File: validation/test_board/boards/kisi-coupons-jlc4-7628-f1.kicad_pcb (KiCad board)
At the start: 4 copper layers, 50 x 96 mm, 16 parts, among them J1 292-J-P-EP-ST-EL-01, J10 292-J-P-EP-ST-EL-01, J11 292-J-P-EP-ST-EL-01, J12 292-J-P-EP-ST-EL-01, J13 292-J-P-EP-ST-EL-01, J14 292-J-P-EP-ST-EL-01, J15 292-J-P-EP-ST-EL-01, J16 292-J-P-EP-ST-EL-01, J2 292-J-P-EP-ST-EL-01, J3 292-J-P-EP-ST-EL-01, J4 292-J-P-EP-ST-EL-01, J5 292-J-P-EP-ST-EL-01, J6 292-J-P-EP-ST-EL-01, J7 292-J-P-EP-ST-EL-01, J8 292-J-P-EP-ST-EL-01, J9 292-J-P-EP-ST-EL-01

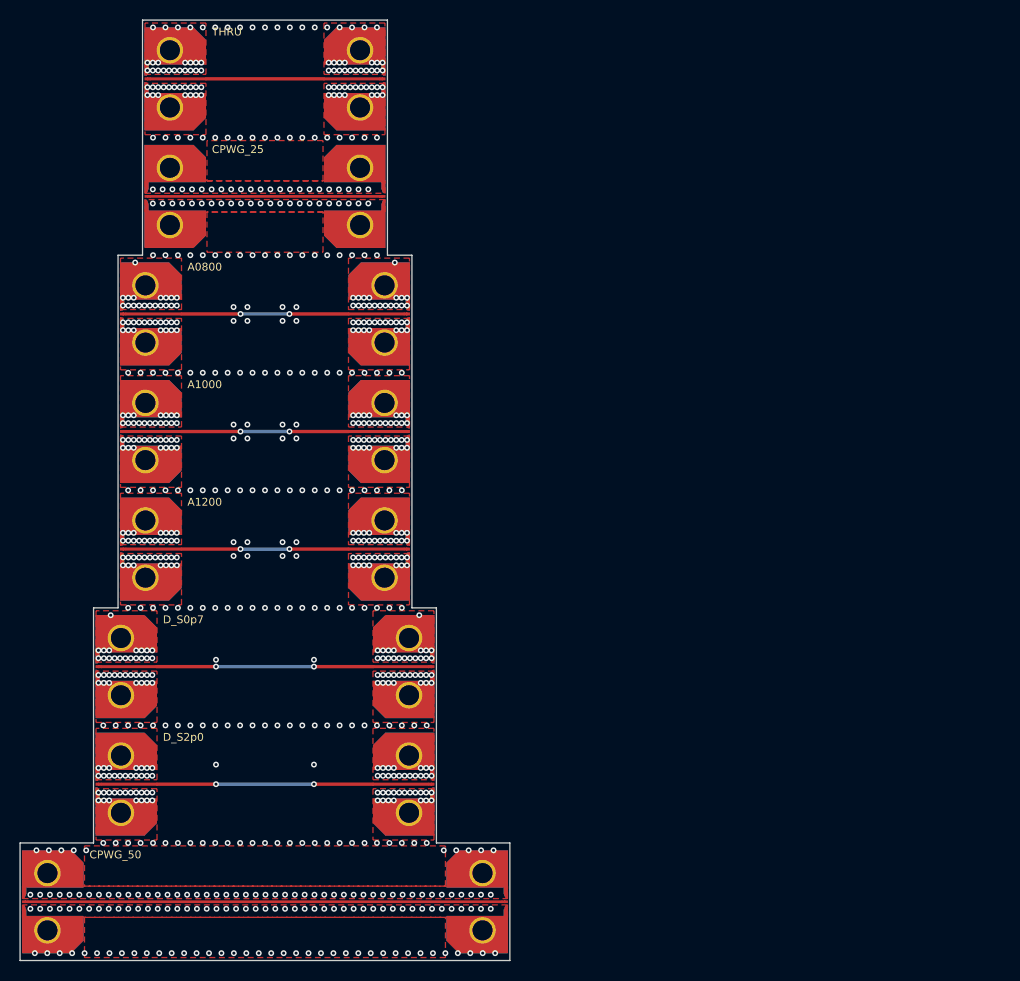
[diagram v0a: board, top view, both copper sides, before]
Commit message: First order: two 4-layer boards and one 6-layer board
- Maintainer's layout (2026-10-31): jlc4-7628-f1 100 x 96 mm (THRU,
  CPWG L / 2L, XT_MS, G_CAV), jlc4-7628-f2 35 x 156 mm (THRU, A x 3,
  D 0.7 / 2 mm / none, PAIR, E with 2 and 0 GND vias), jlc6-7628-f1
  50 x 132 mm (THRU, SL_L3 / VLV_L3, B_L1L6, PAIR, E_R_G2, D x 3). One
  2x-thru per board. An edge launch needs 12 mm of edge per connector
  and side, so the 4-layer set cannot share one 100 x 100 mm board; the
  two boards above their price bracket get their own size limits.
- DRC (KiCad 7, converted copies): no errors; kisi check rerun; the
  first-order table in test_board.md and README lists the exact sizes.

Co-Authored-By: Claude Opus 5.5 <noreply@anthropic.com>
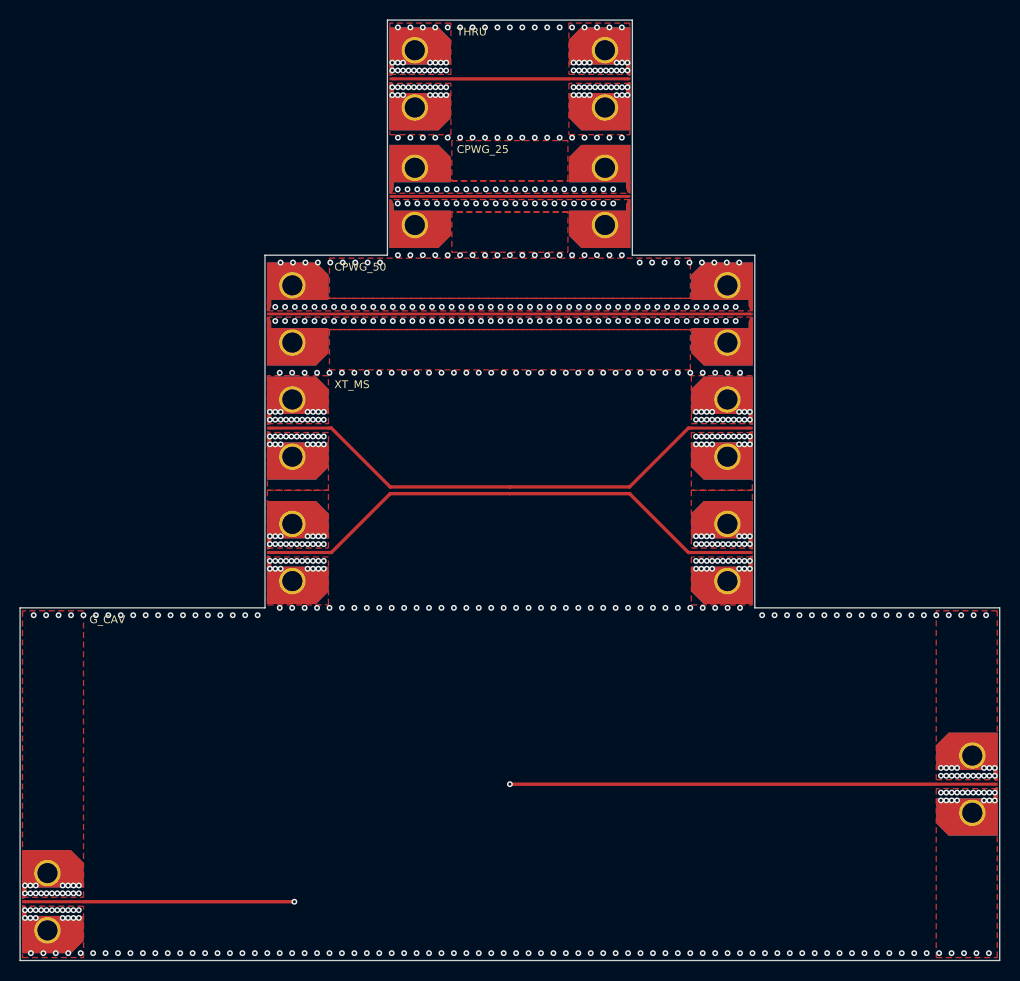
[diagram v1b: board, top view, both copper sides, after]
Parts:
- removed J13, J14, J15, J16: 292-J-P-EP-ST-EL-01, kisi_coupons:Samtec_292-J-P-EP-ST-EL-01_EdgeLaunch
- moved J9 66.2 mm to (105.0, 71.7), turned to 180 degrees
- moved J12 58.7 mm to (130.0, 108.0)
- moved J10 35.0 mm to (105.0, 84.3)
- moved J6 35.0 mm to (105.0, 60.0)
- moved J11 25.1 mm to (30.0, 120.0)
- moved J1 25.0 mm to (67.5, 36.0)
- moved J2 25.0 mm to (92.5, 36.0)
- moved J3 25.0 mm to (67.5, 48.0)
- moved J4 25.0 mm to (92.5, 48.0)
- moved J8 19.4 mm to (55.0, 84.3), turned to 0 degrees
- moved J7 15.0 mm to (55.0, 71.7)
- moved J5 15.0 mm to (55.0, 60.0)
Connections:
- net SE_D_S0p7 renamed CAV_G_CAV
- J10 pad 1: SE_A1200 -> SE_XT_V
- J5 pad 1: SE_A0800 -> SE_CPWG_50
- J6 pad 1: SE_A0800 -> SE_CPWG_50
- J7 pad 1: SE_A1000 -> SE_XT_A
- J8 pad 1: SE_A1000 -> SE_XT_V
- J9 pad 1: SE_A1200 -> SE_XT_A
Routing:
- net SE_XT_V: track 0.00 -> 53.4 mm
- net SE_XT_A: track 0.00 -> 53.4 mm
- net CAV_G_CAV: track 33.4 -> 76.4 mm
- net SE_D_S2p0: track 33.4 -> 0.00 mm, vias 2 -> 0
- net SE_A1200: track 28.4 -> 0.00 mm, vias 2 -> 0
- net SE_A1000: track 28.4 -> 0.00 mm, vias 2 -> 0
- net SE_A0800: track 28.4 -> 0.00 mm, vias 2 -> 0
- net GND: vias 834 -> 697
- added copper zone on In2.Cu, net CAV_G_CAV
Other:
- board size 50 x 96 mm -> 100 x 96 mm
- board text added: "2026-10-31"
- board text added: "G_CAV"
- board text added: "XT_MS"
- board text added: "kisi-coupons-jlc4-7628-f1: kisi measurement coupons v3 (2026-10-31)"
- board text removed: "2026-10-30"
- board text removed: "A0800"
- board text removed: "A1000"
- board text removed: "A1200"
- board text removed: "D_S0p7"
- board text removed: "D_S2p0"
- board text removed: "kisi-coupons-jlc4-7628-f1: kisi measurement coupons v3 (2026-10-30)"

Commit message: Coupon boards: own zone priorities, project-local footprint library
- KiCad 8/9 DRC reported overlapping zones of equal priority (the GND
  pour rectangles on L1 meet at 4-port launch pairs and along the CPWG
  coupons: 78 pairs on 26 boards). Every zone now has its own priority
  (planes 0, pours 1, 2, ..., islands and patches above); an outline
  check finds no equal-priority overlap left.
- The footprints the boards use are written as a project-local library
  (boards/kisi_coupons.pretty + fp-lib-table with ${KIPRJMOD}): the
  Samtec launch per launch width, the capacitor land patterns, the IC
  pin fields; per-instance Port/Status fields dropped, so board and
  library match. DRC (KiCad 7 on converted copies, with the library):
  no library warnings, no errors; the first-order boards are clean.
- Boards regenerated, kisi check unchanged.

Co-Authored-By: Claude Opus 5.5 <noreply@anthropic.com>
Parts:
- removed the J9 at (105.0, 71.7)
- added J8: 292-J-P-EP-ST-EL-01, kisi_coupons:Samtec_292-J-P-EP-ST-EL-01_EdgeLaunch_W0.315, F.Cu at (55.0, 84.3)
- J1, J10, J11, J12, J2, J7: footprint kisi_coupons:Samtec_292-J-P-EP-ST-EL-01_EdgeLaunch -> kisi_coupons:Samtec_292-J-P-EP-ST-EL-01_EdgeLaunch_W0.315
- J3, J4, J5, J6: footprint kisi_coupons:Samtec_292-J-P-EP-ST-EL-01_EdgeLaunch -> kisi_coupons:Samtec_292-J-P-EP-ST-EL-01_EdgeLaunch_W0.28
- J9: renamed from J8; footprint kisi_coupons:Samtec_292-J-P-EP-ST-EL-01_EdgeLaunch -> kisi_coupons:Samtec_292-J-P-EP-ST-EL-01_EdgeLaunch_W0.315
- moved J9 51.6 mm to (105.0, 71.7), turned to 180 degrees
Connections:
- J9 pad 1: SE_XT_V -> SE_XT_A
